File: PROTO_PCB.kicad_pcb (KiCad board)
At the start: 2 copper layers, 83.8 x 50.2 mm, 33 parts, among them J1 12V_IN, J10 12V_AUX, J12 VESC_START, J2 Ethernet connector, J3 SW_KILL_LEFT, J4 SW_KILL_RIGHT, J5 12V_ECU, J8 12V_TEL, J9 12V_HORN, Q1 MOSFET_ECU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

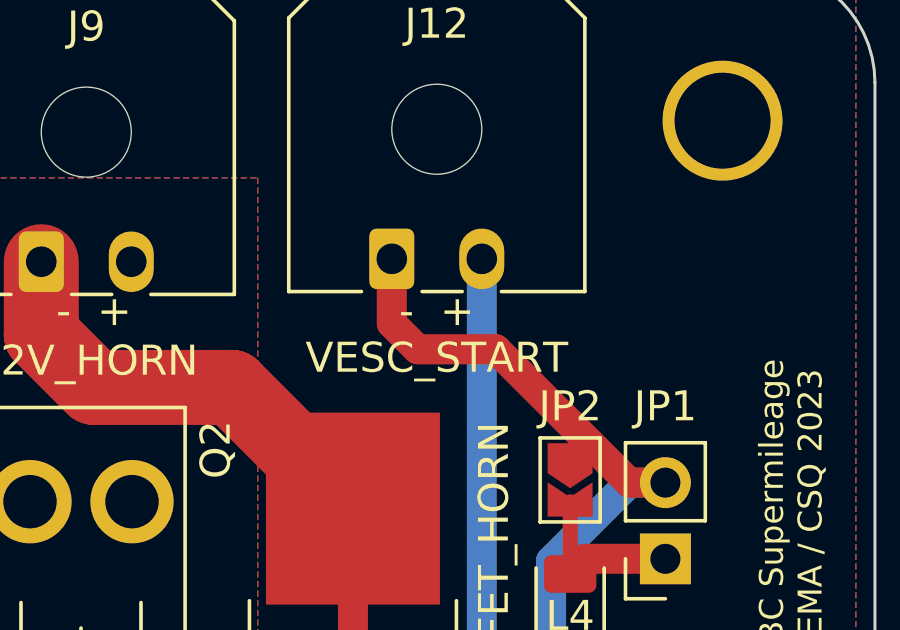
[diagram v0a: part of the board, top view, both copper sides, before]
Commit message: VESC connector labels
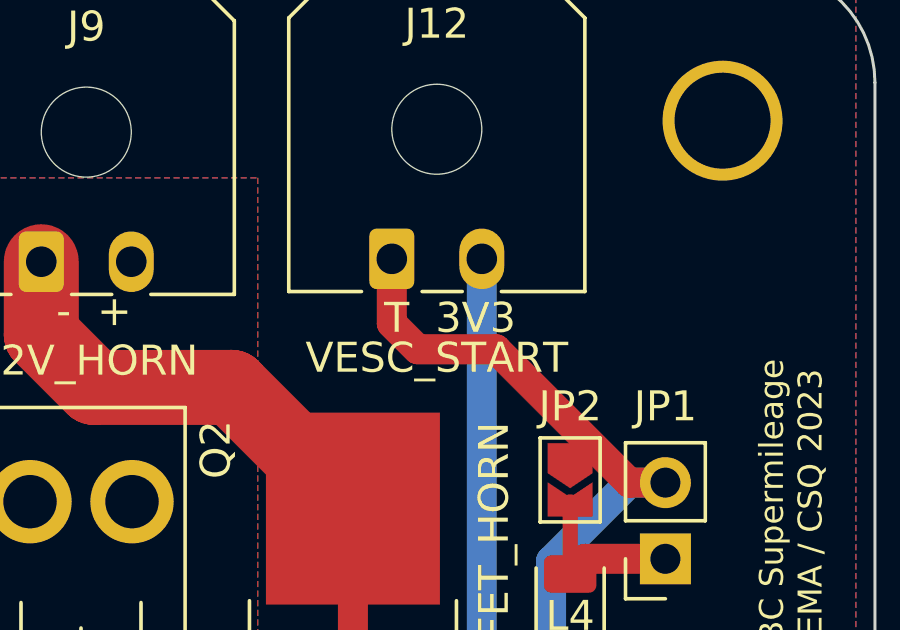
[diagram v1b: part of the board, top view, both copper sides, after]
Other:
- board text added: "T 3V3"
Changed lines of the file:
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@@
     (effects (font (size 2 2) (thickness 0.2)))
   )
-  (gr_text "-  +" (at 110.871 111.125) (layer "F.SilkS")
+  (gr_text "T  3V3" (at 111.310901 111.349354) (layer "F.SilkS")
     (effects (font (size 1 1) (thickness 0.15)))
   )

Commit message: 2023 pcb
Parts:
- added G***: LOGO, LOGO, F.Cu at (117.9, 135.3)
- added G***: LOGO, LOGO, B.Cu at (87.4, 147.0)
- added G***: LOGO, LOGO, B.Cu at (87.9, 130.3)
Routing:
- net Net-(F5-Pad1): track 0.00 -> 18.9 mm
- net GND: track 15.2 -> 31.9 mm
- net Net-(F3-Pad1): track 0.00 -> 15.0 mm
- net +12V: track 38.4 -> 50.8 mm
